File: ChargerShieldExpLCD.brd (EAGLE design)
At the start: 160 x 99.1 mm, 105 parts, among them IC1 TL431, IC2 LM324N, Q1 BUZ11, Q2 BD648, Q3 BUZ171, Q4 IRFZ48Z, T1 BC548, X1 +Vin, X2 VCC, X3 Battery

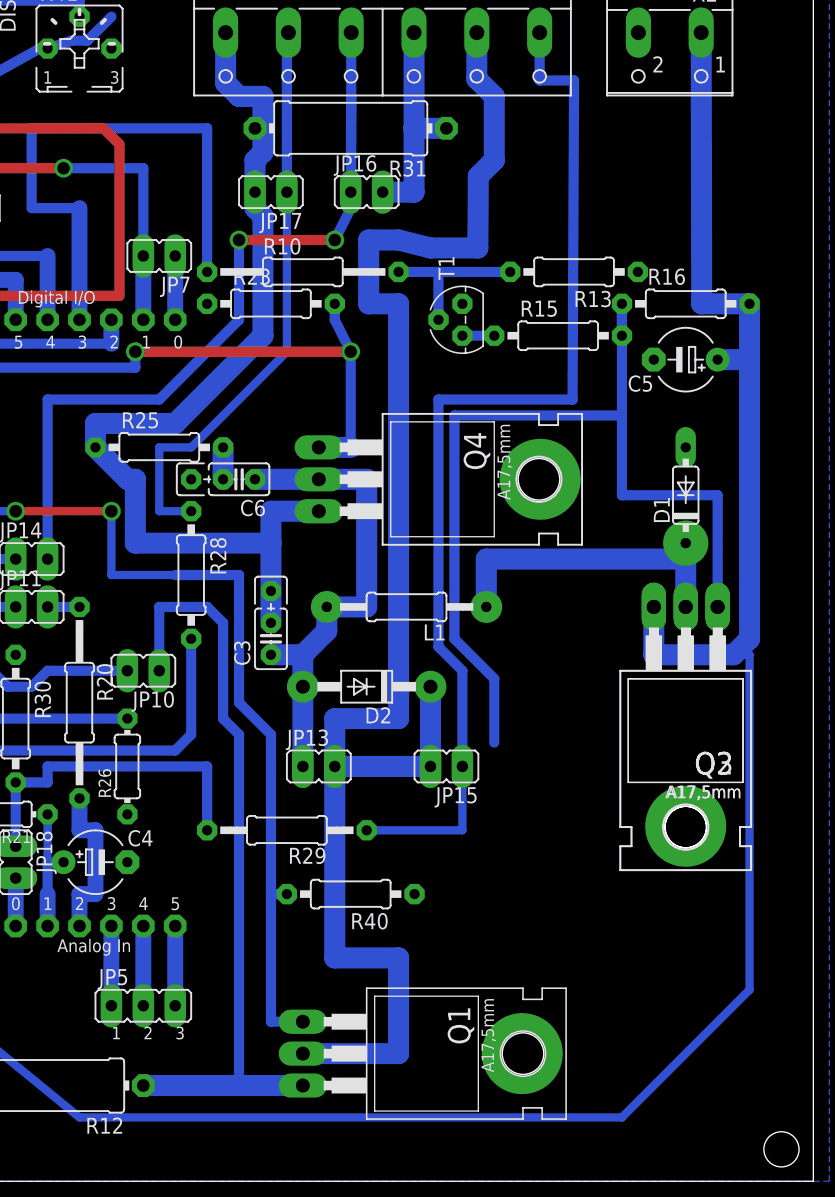
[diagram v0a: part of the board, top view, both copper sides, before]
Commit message: rearranged power transistors
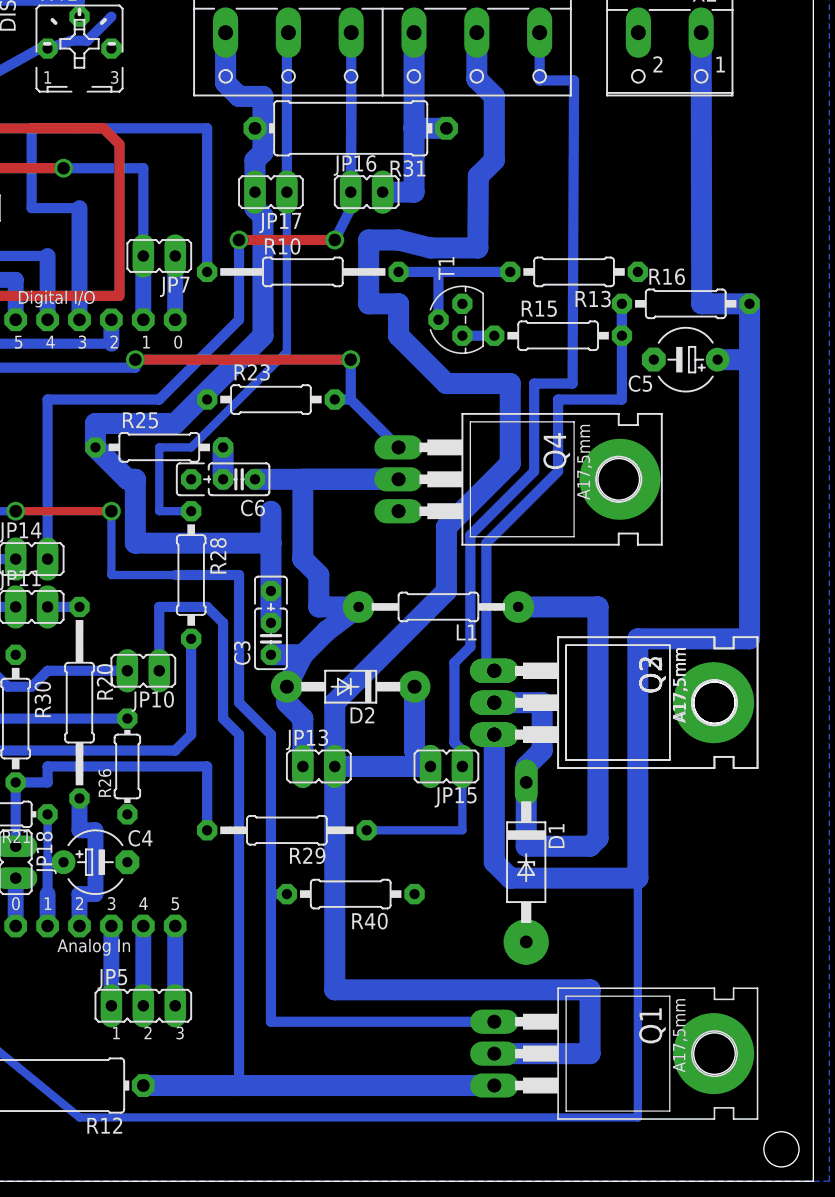
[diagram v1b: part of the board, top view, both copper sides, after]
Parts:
- D1: device diode:DO35-7 -> diode:F126Z12
- moved D1 31.9 mm to (91.4, 7.62), turned to 270 degrees
- moved Q1 15.2 mm to (95.2, -7.62)
- moved Q2 8.98 mm to (95.2, 20.3), turned to 270 degrees
- moved Q3 8.98 mm to (95.2, 20.3), turned to 270 degrees
- moved R23 7.62 mm to (71.1, 44.5)
- moved Q4 6.35 mm to (87.6, 38.1)
- moved L1 2.54 mm to (84.5, 27.9)
- moved D2 1.27 mm to (77.5, 21.6)
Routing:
- net N$7: track 75.0 -> 39.8 mm
- net N$13: track 125.9 -> 149.0 mm
- net N$9: track 26.0 -> 46.5 mm
- net VCC: track 224.7 -> 240.8 mm
- net N$25: track 60.7 -> 76.0 mm
- net N$18: track 85.2 -> 100.4 mm
- net N$10: track 38.3 -> 51.0 mm
- net N$8: track 85.5 -> 80.0 mm
- net N$51: track 46.7 -> 41.6 mm
- net GND: track 169.3 -> 165.5 mm, vias 8 -> 9

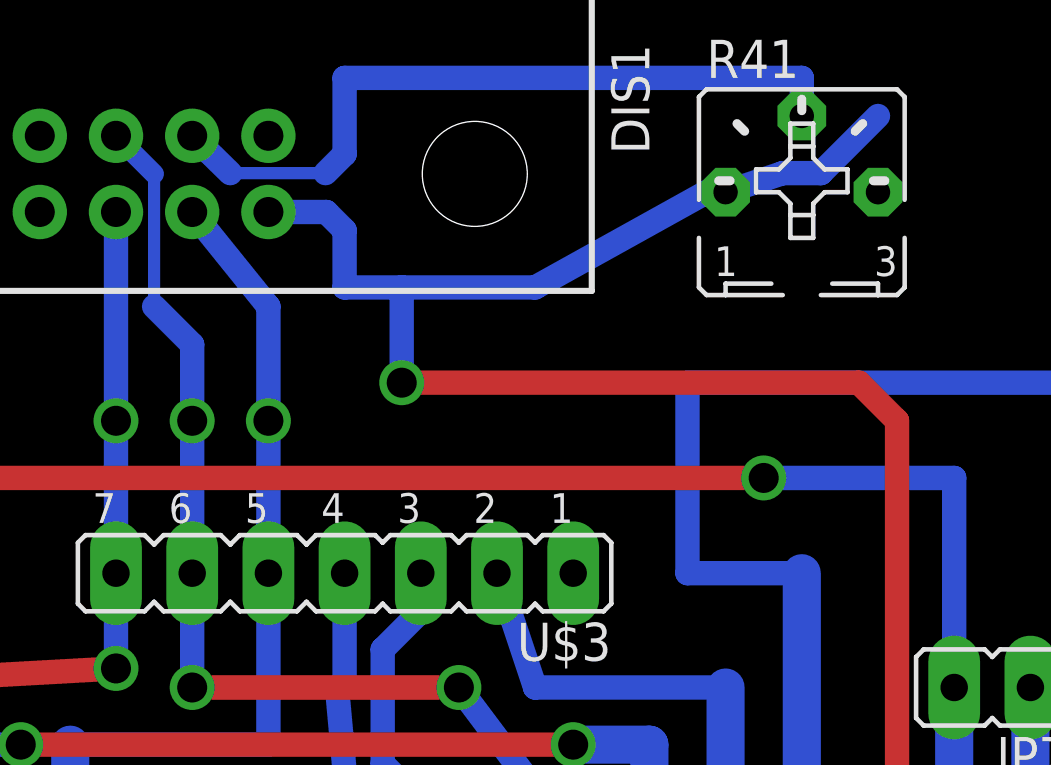
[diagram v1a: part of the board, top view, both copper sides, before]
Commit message: jumper to switch LCD RS Pin
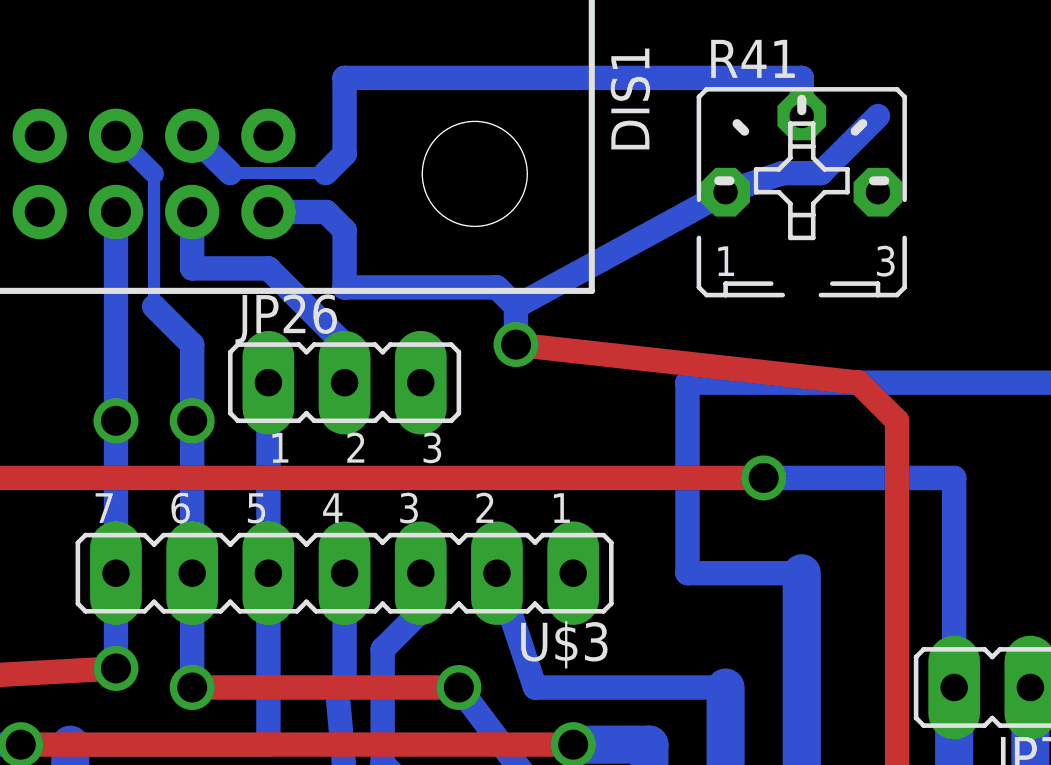
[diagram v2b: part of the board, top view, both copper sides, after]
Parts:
- added JP26: (no value), bigger:JP2
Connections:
- new net N$63: DIS1.4, JP26.2
- net GND: now also JP26.3
- net N$67: now also JP26.1; no longer DIS1.4
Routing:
- net N$63: track 0.00 -> 9.28 mm
- net N$67: track 28.7 -> 22.1 mm, vias 1 -> 0
- net +5V: track 206.5 -> 201.3 mm
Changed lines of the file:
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@@
 </element>
 <element name="R41" library="pot" package="B25P" value="" x="55.88" y="72.39"/>
+<element name="JP26" library="bigger" package="JP2" value="" x="40.64" y="66.04"/>
 </elements>
 <signals>
@@
 <contactref element="R41" pad="E"/>
 <via x="91.44" y="1.27" extent="1-16" drill="0.8" diameter="3.61"/>
+<contactref element="JP26" pad="3"/>
 </signal>
 <signal name="3V">
@@
 <wire x1="40.03" y1="71.73" x2="40.64" y2="71.12" width="0.8128" layer="16"/>
 <wire x1="40.64" y1="71.12" x2="40.64" y2="69.215" width="0.8128" layer="16"/>
-<wire x1="40.64" y1="69.215" x2="42.545" y2="69.215" width="0.8128" layer="16"/>
-<wire x1="42.545" y1="69.215" x2="46.99" y2="69.215" width="0.8128" layer="16"/>
-<wire x1="46.99" y1="69.215" x2="52.705" y2="72.39" width="0.8128" layer="16"/>
-<wire x1="52.705" y1="72.39" x2="53.34" y2="72.39" width="0.8128" layer="16"/>
+<wire x1="40.64" y1="69.215" x2="45.72" y2="69.215" width="0.8128" layer="16"/>
+<wire x1="45.72" y1="69.215" x2="46.355" y2="68.58" width="0.8128" layer="16"/>
+<wire x1="46.355" y1="68.58" x2="53.34" y2="72.39" width="0.8128" layer="16"/>
 <wire x1="53.34" y1="72.39" x2="55.245" y2="73.025" width="0.8128" layer="16"/>
 <wire x1="55.245" y1="73.025" x2="56.515" y2="73.025" width="0.8128" layer="16"/>
@@
 <wire x1="59.055" y1="52.705" x2="59.055" y2="64.77" width="0.8128" layer="1"/>
 <wire x1="59.055" y1="64.77" x2="57.785" y2="66.04" width="0.8128" layer="1"/>
-<wire x1="57.785" y1="66.04" x2="42.545" y2="66.04" width="0.8128" layer="1"/>
-<via x="42.545" y="66.04" extent="1-16" drill="1" shape="square"/>
-<wire x1="42.545" y1="66.04" x2="42.545" y2="69.215" width="0.8128" layer="16"/>
+<wire x1="57.785" y1="66.04" x2="46.355" y2="67.31" width="0.8128" layer="1"/>
+<via x="46.355" y="67.31" extent="1-16" drill="1" shape="square"/>
+<wire x1="46.355" y1="67.31" x2="46.355" y2="68.58" width="0.8128" layer="16"/>
 </signal>
 <signal name="N$5">
@@
 </signal>
 <signal name="N$67">
-<contactref element="DIS1" pad="4"/>
 <contactref element="U$2" pad="D12"/>
 <contactref element="U$3" pad="5"/>
@@
 <wire x1="38.1" y1="53.975" x2="31.496" y2="53.975" width="0.8128" layer="16"/>
 <wire x1="31.496" y1="53.975" x2="31.496" y2="50.8" width="1.27" layer="16"/>
-<wire x1="38.1" y1="59.69" x2="38.1" y2="64.77" width="0.8128" layer="16"/>
-<wire x1="38.1" y1="64.77" x2="38.1" y2="68.58" width="0.8128" layer="16"/>
-<wire x1="38.1" y1="68.58" x2="35.56" y2="71.73" width="0.8128" layer="16"/>
-<via x="38.1" y="64.77" extent="1-16" drill="1" shape="square"/>
+<contactref element="JP26" pad="1"/>
+<wire x1="38.1" y1="66.04" x2="38.1" y2="59.69" width="0.8128" layer="16"/>
 </signal>
 <signal name="N$77">
@@
 <wire x1="55.88" y1="76.2" x2="55.88" y2="74.93" width="0.8128" layer="16"/>
 </signal>
+<signal name="N$63">
+<contactref element="DIS1" pad="4"/>
+<contactref element="JP26" pad="2"/>
+<wire x1="40.64" y1="66.04" x2="40.64" y2="67.31" width="0.8128" layer="16"/>
+<wire x1="40.64" y1="67.31" x2="38.1" y2="69.85" width="0.8128" layer="16"/>
+<wire x1="38.1" y1="69.85" x2="35.56" y2="69.85" width="0.8128" layer="16"/>
+<wire x1="35.56" y1="69.85" x2="35.56" y2="71.73" width="0.8128" layer="16"/>
+</signal>
 </signals>
